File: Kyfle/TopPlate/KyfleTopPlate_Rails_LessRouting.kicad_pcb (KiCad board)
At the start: 2 copper layers, 164 x 146.3 mm, 71 parts, among them SW2 KEY_SWITCH, SW2 PRO MICRO

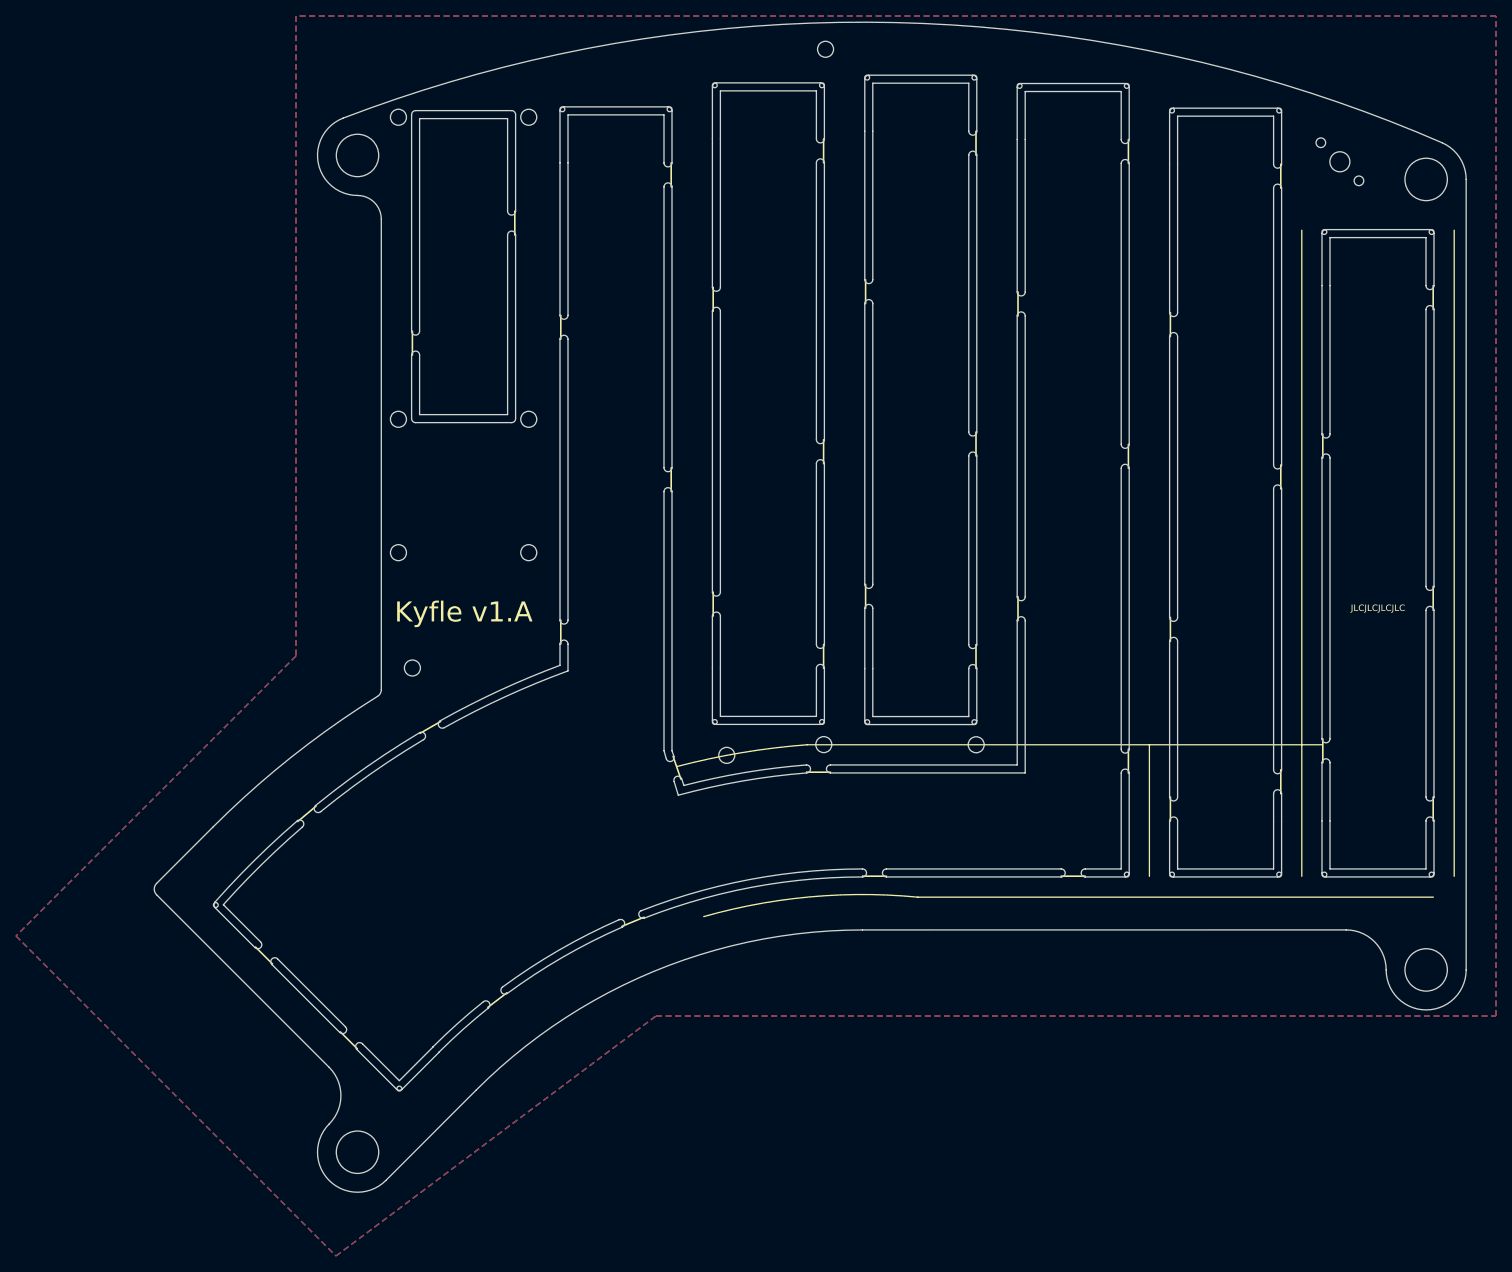
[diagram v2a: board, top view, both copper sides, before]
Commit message: Adds mouse bites to top plate with rails
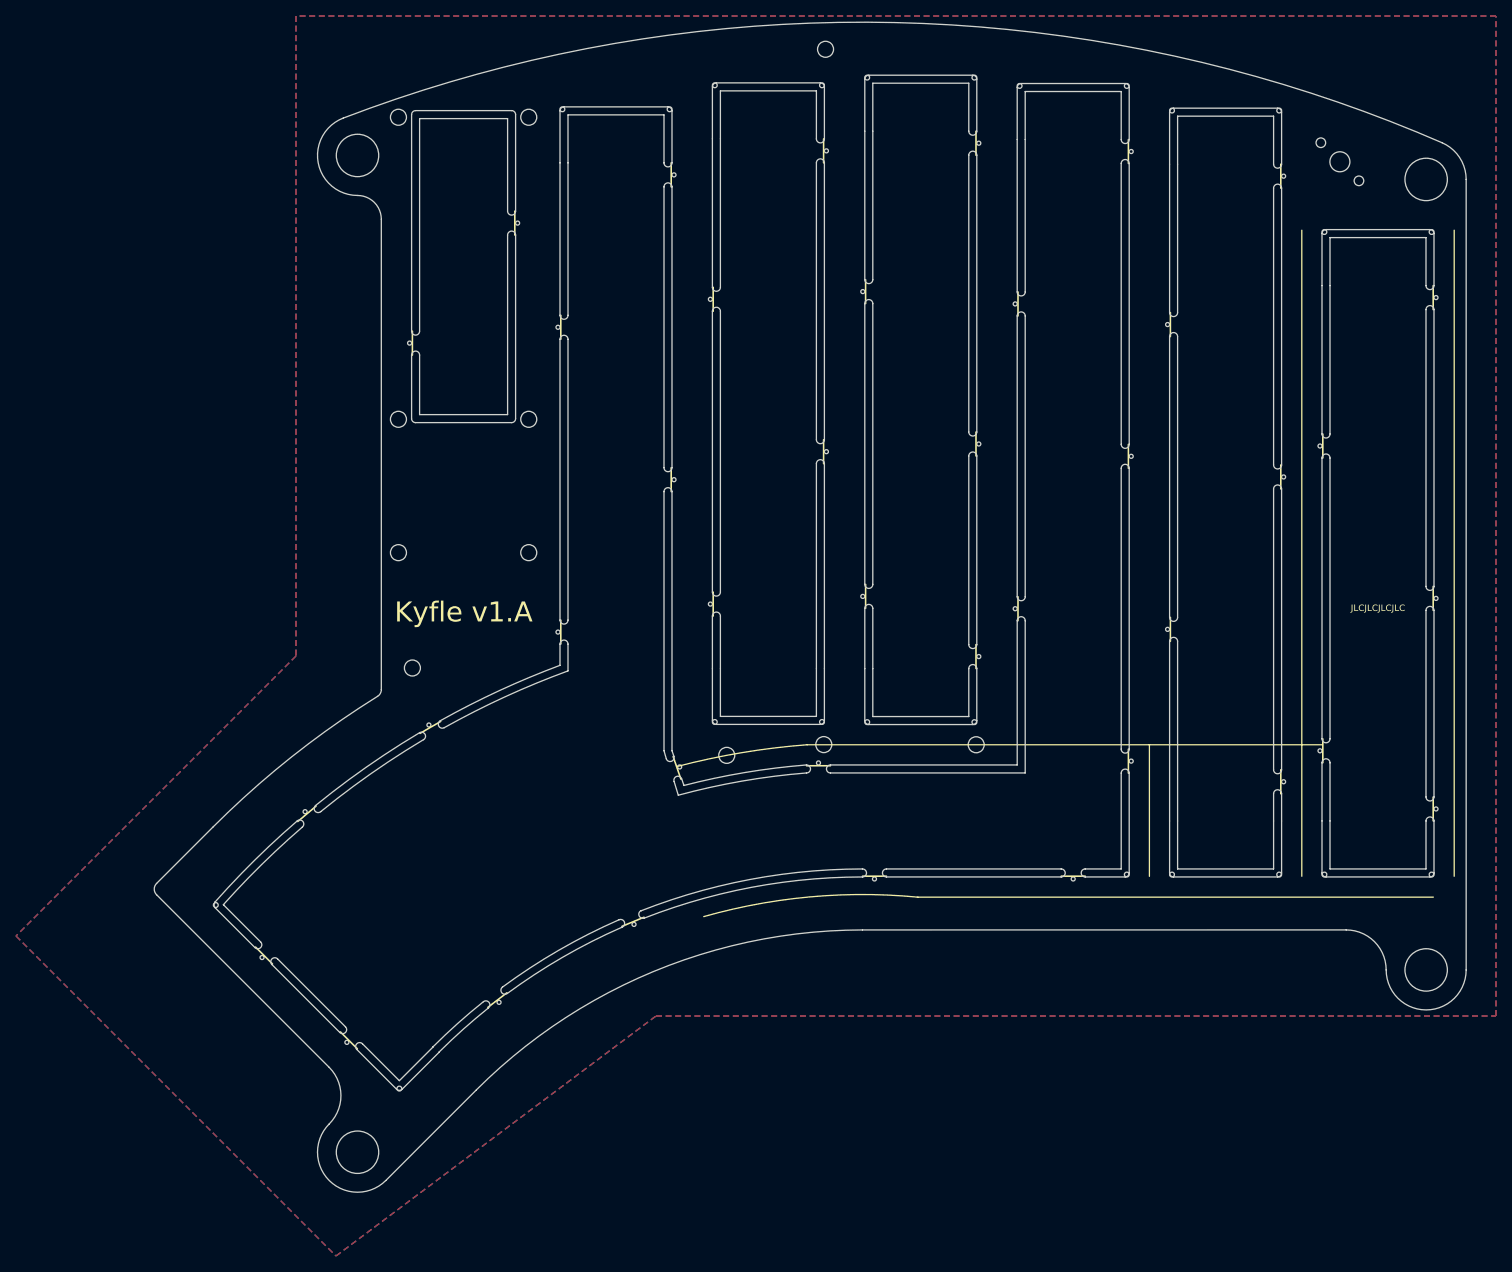
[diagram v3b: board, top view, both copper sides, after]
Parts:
- removed the REF** at (156.5, 97.5)
- removed the REF** at (200.7, 116.6)
- turned REF** to 0 degrees
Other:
- outline, holes or cut-outs redrawn
